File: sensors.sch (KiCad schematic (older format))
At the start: 15 parts, among them U7 BNO055, U8 BMP388, Y2 32.768kHz

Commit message: Final changes for rev.3
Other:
- note added: "Digital pressure sensor"
- note added: "Intelligent 9-axis absolute orientation sensor"
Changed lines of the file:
@@
 Sheet 4 4
 Title "kapukiTRX - Sensors"
-Date "2019-11-09"
-Rev "2"
+Date "2020-01-01"
+Rev "3"
 Comp "bodrico.com"
 Comment1 "Designed by bodri@bodrico.com"
@@
 Wire Wire Line
 	4750 6500 4750 6450
+Text Notes 5500 5950 0    50   ~ 0
+Digital pressure sensor
+Text Notes 6350 2800 0    50   ~ 0
+Intelligent 9-axis absolute orientation sensor
 $EndSCHEMATC

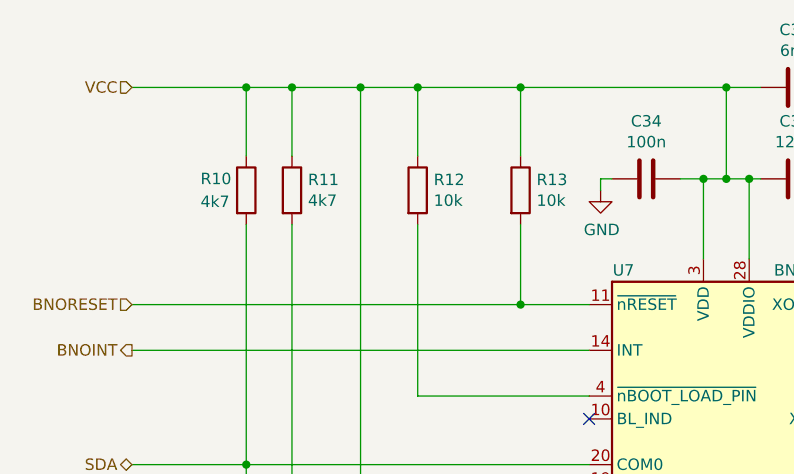
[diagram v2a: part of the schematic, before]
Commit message: Add boot resistor, and fix CAN RX pin
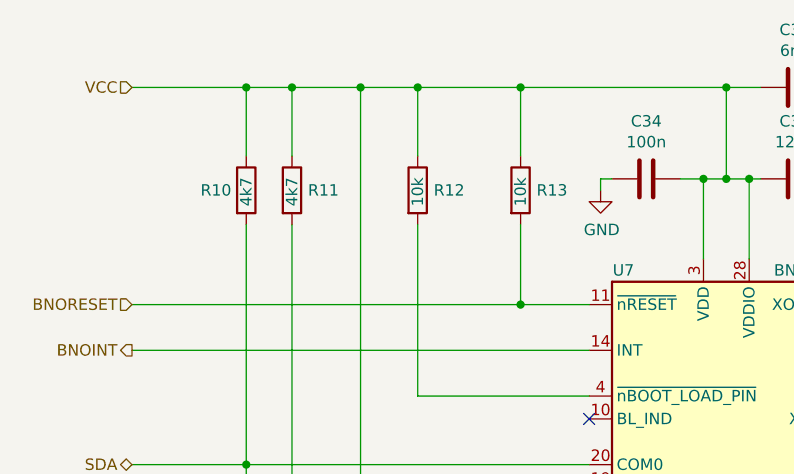
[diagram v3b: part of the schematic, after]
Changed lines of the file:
@@
 Sheet 4 4
 Title "kapukiTRX - Sensors"
-Date "2020-01-01"
-Rev "3"
+Date "2020-03-29"
+Rev "4"
 Comp "bodrico.com"
 Comment1 "Designed by bodri@bodrico.com"
@@
 U 1 1 5DB9719F
 P 3250 1800
-F 0 "R12" H 3320 1846 50  0000 L CNN
-F 1 "10k" H 3320 1755 50  0000 L CNN
+F 0 "R12" H 3320 1800 50  0000 L CNN
+F 1 "10k" V 3250 1730 50  0000 L CNN
 F 2 "Resistor_SMD:R_0402_1005Metric" V 3180 1800 50  0001 C CNN
 F 3 "~" H 3250 1800 50  0001 C CNN
@@
 U 1 1 5DB9A969
 P 2500 1800
-F 0 "R10" H 2300 1850 50  0000 L CNN
-F 1 "4k7" H 2300 1750 50  0000 L CNN
+F 0 "R10" H 2300 1800 50  0000 L CNN
+F 1 "4k7" V 2500 1730 50  0000 L CNN
 F 2 "Resistor_SMD:R_0402_1005Metric" V 2430 1800 50  0001 C CNN
 F 3 "~" H 2500 1800 50  0001 C CNN
@@
 U 1 1 5DB9AE9A
 P 2700 1800
-F 0 "R11" H 2770 1846 50  0000 L CNN
-F 1 "4k7" H 2770 1755 50  0000 L CNN
+F 0 "R11" H 2770 1800 50  0000 L CNN
+F 1 "4k7" V 2700 1730 50  0000 L CNN
 F 2 "Resistor_SMD:R_0402_1005Metric" V 2630 1800 50  0001 C CNN
 F 3 "~" H 2700 1800 50  0001 C CNN
@@
 U 1 1 5DC52129
 P 3700 1800
-F 0 "R13" H 3770 1846 50  0000 L CNN
-F 1 "10k" H 3770 1755 50  0000 L CNN
+F 0 "R13" H 3770 1800 50  0000 L CNN
+F 1 "10k" V 3700 1730 50  0000 L CNN
 F 2 "Resistor_SMD:R_0402_1005Metric" V 3630 1800 50  0001 C CNN
 F 3 "~" H 3700 1800 50  0001 C CNN

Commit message: Add pull-up for uart
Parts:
- U7: symbol Sensor_Motion:BNO055 -> kapukiTRX-hw-trx-rescue:BNO055-Sensor_Motion
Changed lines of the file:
@@
 $EndDescr
 $Comp
-L Sensor_Motion:BNO055 U7
+L kapukiTRX-hw-trx-rescue:BNO055-Sensor_Motion U7
 U 1 1 5DB894CB
 P 4600 2800
+AR Path="/5DB894CB" Ref="U7"  Part="1"
+AR Path="/5DB88B39/5DB894CB" Ref="U7"  Part="1"
 F 0 "U7" H 4150 3450 50  0000 C CNN
 F 1 "BNO055" H 4950 3450 50  0000 C CNN

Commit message: Make some value changes for consistency
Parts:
- C33, C34, C37, C38: value 100n -> 100nF
- C35: value 6n8 -> 6.8nF
- C36: value 120n -> 120nF
- C39, C40: value 22p -> 22pF
- U7: symbol kapukiTRX-hw-trx-rescue:BNO055-Sensor_Motion -> kapukiTRX-hw-trx-rescue:BNO055-Sensor_Motion-kapukiTRX-hw-trx-rescue
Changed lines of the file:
@@
 EESchema Schematic File Version 4
-LIBS:kapukiTRX-hw-trx-cache
 EELAYER 30 0
 EELAYER END
@@
 $EndDescr
 $Comp
-L kapukiTRX-hw-trx-rescue:BNO055-Sensor_Motion U7
+L kapukiTRX-hw-trx-rescue:BNO055-Sensor_Motion-kapukiTRX-hw-trx-rescue U7
 U 1 1 5DB894CB
 P 4600 2800
@@
 P 5300 3550
 F 0 "C38" H 5415 3596 50  0000 L CNN
-F 1 "100n" H 5415 3505 50  0000 L CNN
+F 1 "100nF" H 5415 3505 50  0000 L CNN
 F 2 "Capacitor_SMD:C_0402_1005Metric" H 5338 3400 50  0001 C CNN
 F 3 "~" H 5300 3550 50  0001 C CNN
 	1    5300 3550
 	1    0    0    -1
-$EndComp
-$Comp
-L Device:C C36
-U 1 1 5DB8BA5D
-P 4900 1750
-F 0 "C36" V 4648 1750 50  0000 C CNN
-F 1 "120n" V 4739 1750 50  0000 C CNN
-F 2 "Capacitor_SMD:C_0402_1005Metric" H 4938 1600 50  0001 C CNN
-F 3 "~" H 4900 1750 50  0001 C CNN
-	1    4900 1750
-	0    1    1    0
 $EndComp
 $Comp
@@
 P 5850 2300
 F 0 "C39" V 5598 2300 50  0000 C CNN
-F 1 "22p" V 5689 2300 50  0000 C CNN
+F 1 "22pF" V 5689 2300 50  0000 C CNN
 F 2 "Capacitor_SMD:C_0402_1005Metric" H 5888 2150 50  0001 C CNN
 F 3 "~" H 5850 2300 50  0001 C CNN
@@
 P 4950 5150
 F 0 "C37" V 4698 5150 50  0000 C CNN
-F 1 "100n" V 4789 5150 50  0000 C CNN
+F 1 "100nF" V 4789 5150 50  0000 C CNN
 F 2 "Capacitor_SMD:C_0402_1005Metric" H 4988 5000 50  0001 C CNN
 F 3 "~" H 4950 5150 50  0001 C CNN
@@
 P 3850 5150
 F 0 "C33" V 3598 5150 50  0000 C CNN
-F 1 "100n" V 3689 5150 50  0000 C CNN
+F 1 "100nF" V 3689 5150 50  0000 C CNN
 F 2 "Capacitor_SMD:C_0402_1005Metric" H 3888 5000 50  0001 C CNN
 F 3 "~" H 3850 5150 50  0001 C CNN
@@
 P 4900 1350
 F 0 "C35" V 4648 1350 50  0000 C CNN
-F 1 "6n8" V 4739 1350 50  0000 C CNN
+F 1 "6.8nF" V 4739 1350 50  0000 C CNN
 F 2 "Capacitor_SMD:C_0402_1005Metric" H 4938 1200 50  0001 C CNN
 F 3 "~" H 4900 1350 50  0001 C CNN
@@
 Wire Wire Line
 	3250 1350 3250 1650
-$Comp
-L Device:C C34
-U 1 1 5DBEF9AF
-P 4250 1750
-F 0 "C34" V 3998 1750 50  0000 C CNN
-F 1 "100n" V 4089 1750 50  0000 C CNN
-F 2 "Capacitor_SMD:C_0402_1005Metric" H 4288 1600 50  0001 C CNN
-F 3 "~" H 4250 1750 50  0001 C CNN
-	1    4250 1750
-	0    1    1    0
-$EndComp
 $Comp
 L power:GND #PWR0109
@@
 P 5850 2800
 F 0 "C40" V 5800 2650 50  0000 C CNN
-F 1 "22p" V 6000 2800 50  0000 C CNN
+F 1 "22pF" V 6000 2800 50  0000 C CNN
 F 2 "Capacitor_SMD:C_0402_1005Metric" H 5888 2650 50  0001 C CNN
 F 3 "~" H 5850 2800 50  0001 C CNN
@@
 Text Notes 6350 2800 0    50   ~ 0
 Intelligent 9-axis absolute orientation sensor
+$Comp
+L Device:C C34
+U 1 1 5DBEF9AF
+P 4250 1750
+F 0 "C34" V 3998 1750 50  0000 C CNN
+F 1 "100nF" V 4089 1750 50  0000 C CNN
+F 2 "Capacitor_SMD:C_0402_1005Metric" H 4288 1600 50  0001 C CNN
+F 3 "~" H 4250 1750 50  0001 C CNN
+	1    4250 1750
+	0    1    1    0
+$EndComp
+$Comp
+L Device:C C36
+U 1 1 5DB8BA5D
+P 4900 1750
+F 0 "C36" V 4648 1750 50  0000 C CNN
+F 1 "120nF" V 4739 1750 50  0000 C CNN
+F 2 "Capacitor_SMD:C_0402_1005Metric" H 4938 1600 50  0001 C CNN
+F 3 "~" H 4900 1750 50  0001 C CNN
+	1    4900 1750
+	0    1    1    0
+$EndComp
 $EndSCHEMATC
